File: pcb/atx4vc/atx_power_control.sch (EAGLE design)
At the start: 59 parts, among them IC2 REG1117, IC3 STM32F042F4, IC4 MY_7905DT, J1 ATX24RH, SW1 324_SW, SW2 324_SW, SW3 324_SW, SW4 324_SW, SW5 324_SW, SW7 324_SW, U1 USBC_16P, U2 USBC_16P

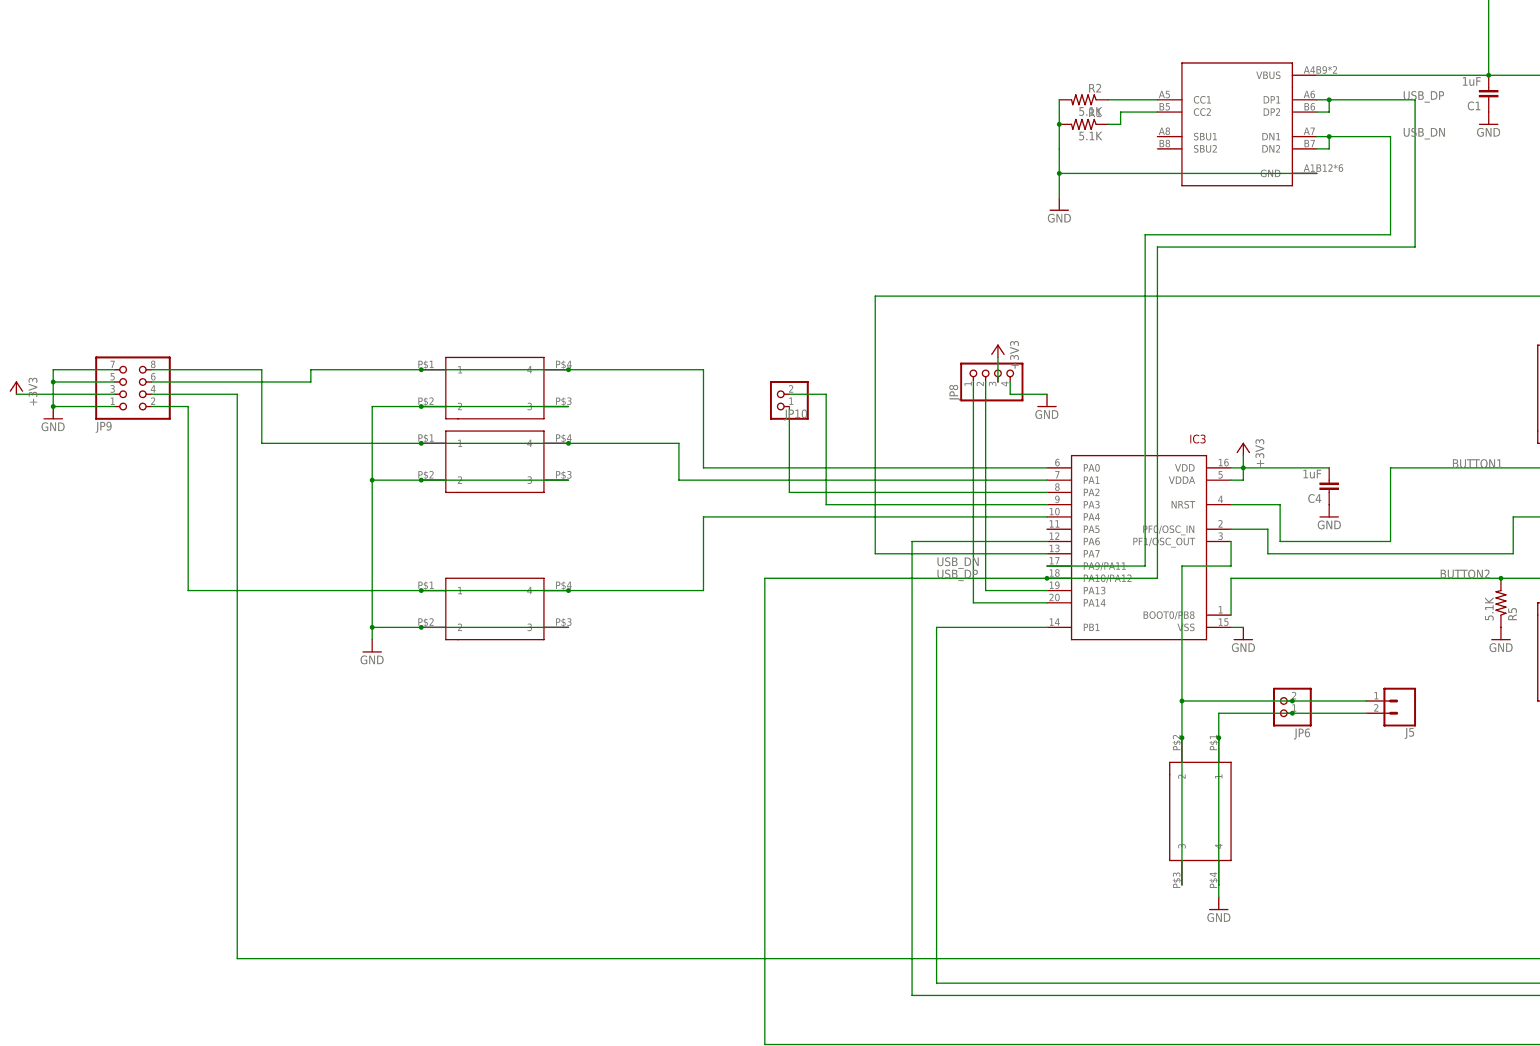
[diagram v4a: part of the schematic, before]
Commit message: optimised traces routing for current carrying
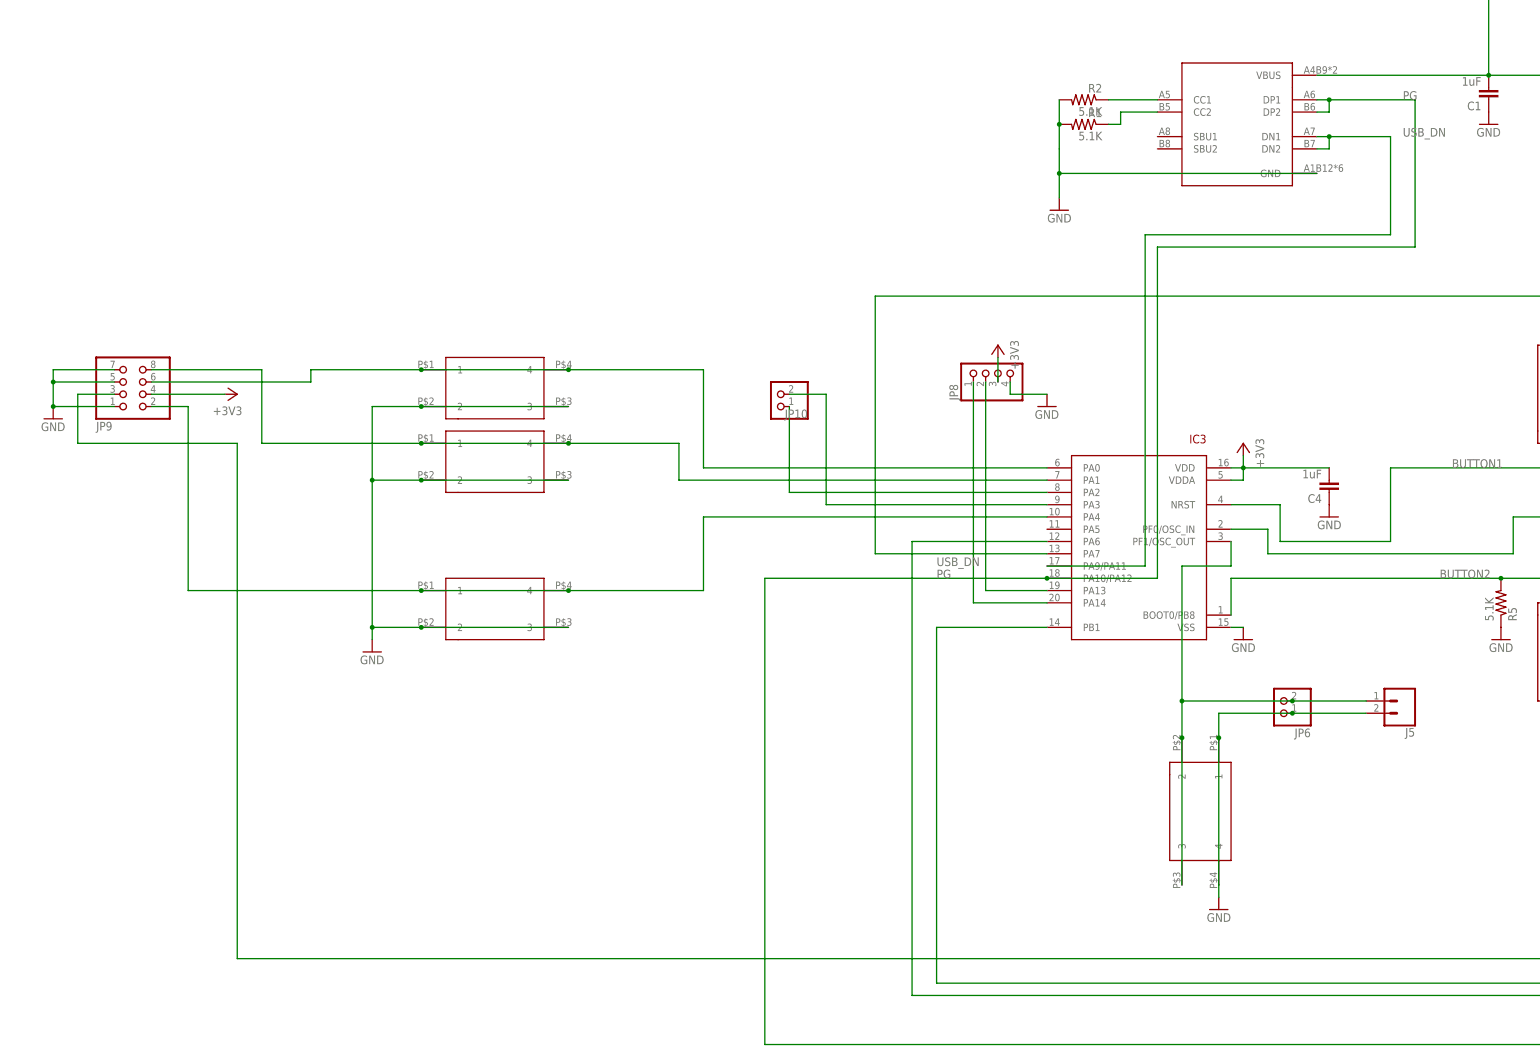
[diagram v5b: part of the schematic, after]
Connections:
- net USB_DP renamed PG
- net +3V3: now also JP9.4; no longer JP9.3
- net BUTTON2: now also JP9.3; no longer JP9.4
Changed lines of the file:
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@@
 <attribute name="VALUE" x="243.84" y="101.6" size="1.778" layer="96" rot="MR0"/>
 </instance>
-<instance part="+3V3" gate="G$1" x="-231.14" y="58.42" smashed="yes" rot="MR0">
-<attribute name="VALUE" x="-228.6" y="53.34" size="1.778" layer="96" rot="MR90"/>
+<instance part="+3V3" gate="G$1" x="-185.42" y="55.88" smashed="yes" rot="MR90">
+<attribute name="VALUE" x="-190.5" y="53.34" size="1.778" layer="96" rot="MR180"/>
 </instance>
 <instance part="R12" gate="G$1" x="327.66" y="71.12" smashed="yes" rot="R270">
@@
 </segment>
 <segment>
-<pinref part="JP9" gate="A" pin="3"/>
+<pinref part="JP9" gate="A" pin="4"/>
 <pinref part="+3V3" gate="G$1" pin="+3V3"/>
-<wire x1="-210.82" y1="55.88" x2="-231.14" y2="55.88" width="0.1524" layer="91"/>
+<wire x1="-203.2" y1="55.88" x2="-187.96" y2="55.88" width="0.1524" layer="91"/>
 </segment>
 </net>
@@
 <wire x1="86.36" y1="-60.96" x2="-185.42" y2="-60.96" width="0.1524" layer="91"/>
 <junction x="86.36" y="-12.7"/>
-<wire x1="-185.42" y1="55.88" x2="-203.2" y2="55.88" width="0.1524" layer="91"/>
-<pinref part="JP9" gate="A" pin="4"/>
-<wire x1="-185.42" y1="-60.96" x2="-185.42" y2="55.88" width="0.1524" layer="91"/>
+<wire x1="-185.42" y1="-60.96" x2="-185.42" y2="45.72" width="0.1524" layer="91"/>
+<pinref part="JP9" gate="A" pin="3"/>
+<wire x1="-210.82" y1="55.88" x2="-218.44" y2="55.88" width="0.1524" layer="91"/>
+<wire x1="-218.44" y1="55.88" x2="-218.44" y2="45.72" width="0.1524" layer="91"/>
+<wire x1="-218.44" y1="45.72" x2="-185.42" y2="45.72" width="0.1524" layer="91"/>
 </segment>
 </net>
@@
 </segment>
 </net>
-<net name="USB_DP" class="0">
+<net name="PG" class="0">
 <segment>
 <pinref part="U2" gate="G$1" pin="DP2"/>
